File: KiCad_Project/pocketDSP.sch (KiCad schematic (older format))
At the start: 103 parts, among them IC1 TP4056, J2 USB_B_Micro, J3 SJ1-3525N, J4 SJ1-3525N, SW2 SW_SPDT, SW3 SW_SPDT, U1 3.5\"_TFT_LCD_SHILD_TOUCHSCRE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, U2 STM32H743VITx, U3 LMR62014XMF, U4 AP1117-33, U5 LM358, U6 CS5341, U7 CS4345, U8 LM358, Y1 25MHz

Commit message: V1.0
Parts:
- U5, U8: value LM358 -> OPA2340
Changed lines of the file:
@@
 P 7900 5700
 F 0 "U5" H 7900 6067 50  0000 C CNN
-F 1 "LM358" H 7900 5976 50  0000 C CNN
+F 1 "OPA2340" H 7900 5976 50  0000 C CNN
 F 2 "Package_SO:SOIC-8_3.9x4.9mm_P1.27mm" H 7900 5700 50  0001 C CNN
 F 3 "http://www.ti.com/lit/ds/symlink/lm2904-n.pdf" H 7900 5700 50  0001 C CNN
@@
 P 7900 4200
 F 0 "U5" H 7900 4550 50  0000 C CNN
-F 1 "LM358" H 7900 4450 50  0000 C CNN
+F 1 "OPA2340" H 7900 4450 50  0000 C CNN
 F 2 "Package_SO:SOIC-8_3.9x4.9mm_P1.27mm" H 7900 4200 50  0001 C CNN
 F 3 "http://www.ti.com/lit/ds/symlink/lm2904-n.pdf" H 7900 4200 50  0001 C CNN
@@
 P 6400 5650
 F 0 "U5" H 6358 5696 50  0000 L CNN
-F 1 "LM358" H 6358 5605 50  0000 L CNN
+F 1 "OPA2340" H 6358 5605 50  0000 L CNN
 F 2 "Package_SO:SOIC-8_3.9x4.9mm_P1.27mm" H 6400 5650 50  0001 C CNN
 F 3 "http://www.ti.com/lit/ds/symlink/lm2904-n.pdf" H 6400 5650 50  0001 C CNN
@@
 P 9900 5400
 F 0 "U8" H 9900 5767 50  0000 C CNN
-F 1 "LM358" H 9900 5676 50  0000 C CNN
+F 1 "OPA2340" H 9900 5676 50  0000 C CNN
 F 2 "Package_SO:SOIC-8_3.9x4.9mm_P1.27mm" H 9900 5400 50  0001 C CNN
 F 3 "http://www.ti.com/lit/ds/symlink/lm2904-n.pdf" H 9900 5400 50  0001 C CNN
@@
 P 9900 3900
 F 0 "U8" H 9900 4250 50  0000 C CNN
-F 1 "LM358" H 9900 4150 50  0000 C CNN
+F 1 "OPA2340" H 9900 4150 50  0000 C CNN
 F 2 "Package_SO:SOIC-8_3.9x4.9mm_P1.27mm" H 9900 3900 50  0001 C CNN
 F 3 "http://www.ti.com/lit/ds/symlink/lm2904-n.pdf" H 9900 3900 50  0001 C CNN
@@
 P 12450 5800
 F 0 "U8" H 12408 5846 50  0000 L CNN
-F 1 "LM358" H 12408 5755 50  0000 L CNN
+F 1 "OPA2340" H 12408 5755 50  0000 L CNN
 F 2 "Package_SO:SOIC-8_3.9x4.9mm_P1.27mm" H 12450 5800 50  0001 C CNN
 F 3 "http://www.ti.com/lit/ds/symlink/lm2904-n.pdf" H 12450 5800 50  0001 C CNN

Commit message: v1.0
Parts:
- L2, L3: footprint Inductor_SMD:L_1210_3225Metric_Pad1.42x2.65mm_HandSolder -> Inductor_SMD:L_Coilcraft_LPS5030
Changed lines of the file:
@@
 F 0 "L3" V 1290 10400 50  0000 C CNN
 F 1 "10uH" V 1199 10400 50  0000 C CNN
-F 2 "Inductor_SMD:L_1210_3225Metric_Pad1.42x2.65mm_HandSolder" H 1100 10400 50  0001 C CNN
+F 2 "Inductor_SMD:L_Coilcraft_LPS5030" H 1100 10400 50  0001 C CNN
 F 3 "~" H 1100 10400 50  0001 C CNN
 	1    1100 10400
@@
 F 0 "L2" V 3140 8800 50  0000 C CNN
 F 1 "10uH" V 3049 8800 50  0000 C CNN
-F 2 "Inductor_SMD:L_1210_3225Metric_Pad1.42x2.65mm_HandSolder" H 2950 8800 50  0001 C CNN
+F 2 "Inductor_SMD:L_Coilcraft_LPS5030" H 2950 8800 50  0001 C CNN
 F 3 "~" H 2950 8800 50  0001 C CNN
 	1    2950 8800

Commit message: v1.1
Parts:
- removed C10, C24, C7, C8, C9: 100nF, Capacitor_SMD:C_0402_1005Metric, symbol Device:C
- removed L3: 10uH, Inductor_SMD:L_Coilcraft_LPS5030, symbol Device:L
- added J1, J5: Conn_01x01, TestPoint:TestPoint_Pad_3.0x3.0mm, symbol Connector_Generic:Conn_01x01
- added MK1: Mic, Connector_Audio:CUI_CMA-6542PF, symbol Device:Microphone_Condenser
- added R26, R27: 100k, Resistor_SMD:R_0805_2012Metric_Pad1.15x1.40mm_HandSolder, symbol Device:R
- added SW1: SW_Push, Button_Switch_SMD:SW_SPST_CK_KXT3, symbol Switch:SW_Push
- C1, C13, C14, C15, C17, C18, C2, C20, C22, C26, C28, C29, C30, C31, C32, C33, C34, C35, C36, C37, C38, C39, C4, C40, C41, C42, C43, C44, C45, C46, C47, C48, C49, C5, C50, C51, C52, C53, C54: footprint Capacitor_SMD:C_0402_1005Metric -> Capacitor_SMD:C_0805_2012Metric_Pad1.15x1.40mm_HandSolder
- C12, C16, C19, C25: value 2.2uF -> 10uF
- C21: value 100nF -> 10uF; footprint Capacitor_SMD:C_0402_1005Metric -> Capacitor_SMD:C_0805_2012Metric_Pad1.15x1.40mm_HandSolder
- C23: value 2.2uF -> 100n
- C3, C6: value 100n -> 10uF; footprint Capacitor_SMD:C_0402_1005Metric -> Capacitor_SMD:C_0805_2012Metric_Pad1.15x1.40mm_HandSolder
- L1: value 10uH -> 1uH
- R1, R11, R12, R13, R14, R15, R16, R17, R18, R19, R2, R20, R21, R22, R23, R24, R25, R3, R4, R5, R6, R7, R8, R9: footprint Resistor_SMD:R_0402_1005Metric -> Resistor_SMD:R_0805_2012Metric_Pad1.15x1.40mm_HandSolder
- R10: value 3.3k -> 2.2k; footprint Resistor_SMD:R_0402_1005Metric -> Resistor_SMD:R_0805_2012Metric_Pad1.15x1.40mm_HandSolder
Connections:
- net +3V3: now also R26.1
- net +5V: now also U4.3 (VI)
- net ADC_AINL: now also C42.2, R18.1, R20.2; no longer C41.2, R17.1, R19.2
- net ADC_AINR: now also C41.2, R17.1, R19.2; no longer C42.2, R18.1, R20.2
- net ADC_M1: now also U2.57 (PD10); no longer U2.56 (PD9)
- net ADC_RST: now also U2.56 (PD9); no longer U2.57 (PD10)
- net GND: now also J5.1 (Pin_1), MK1.1 (-), R27.1, SW1.1
- net L_IN: now also C36.2, R12.2; no longer C35.2, R11.2
- net L_OUT: now also J4.3; no longer J4.2
- net R_IN: now also C35.2, R11.2; no longer C36.2, R12.2
- net R_OUT: now also J4.2; no longer J4.3
- net USB_5V: now also D2.2 (A), D4.2 (A); no longer R6.1, R9.1
- net at C15.1, U2.14 (NRST): now also SW1.2
- net MIC_IN: now reaches U2.16 (PC1)
- net MIC_IN: now also MK1.2 (+), R26.2, R27.2
- net at IC1.6 (STDBY): now also R9.2; no longer D4.1 (K)
- net at IC1.7 (CHRG): now also R6.2; no longer D2.1 (K)
- net at BT1.+, F1.2: now also J1.1 (Pin_1)
- new net: D2.1 (K), R6.1
- new net: D4.1 (K), R9.1
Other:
- moved on the sheet: C23, D2, D4, R6, R9

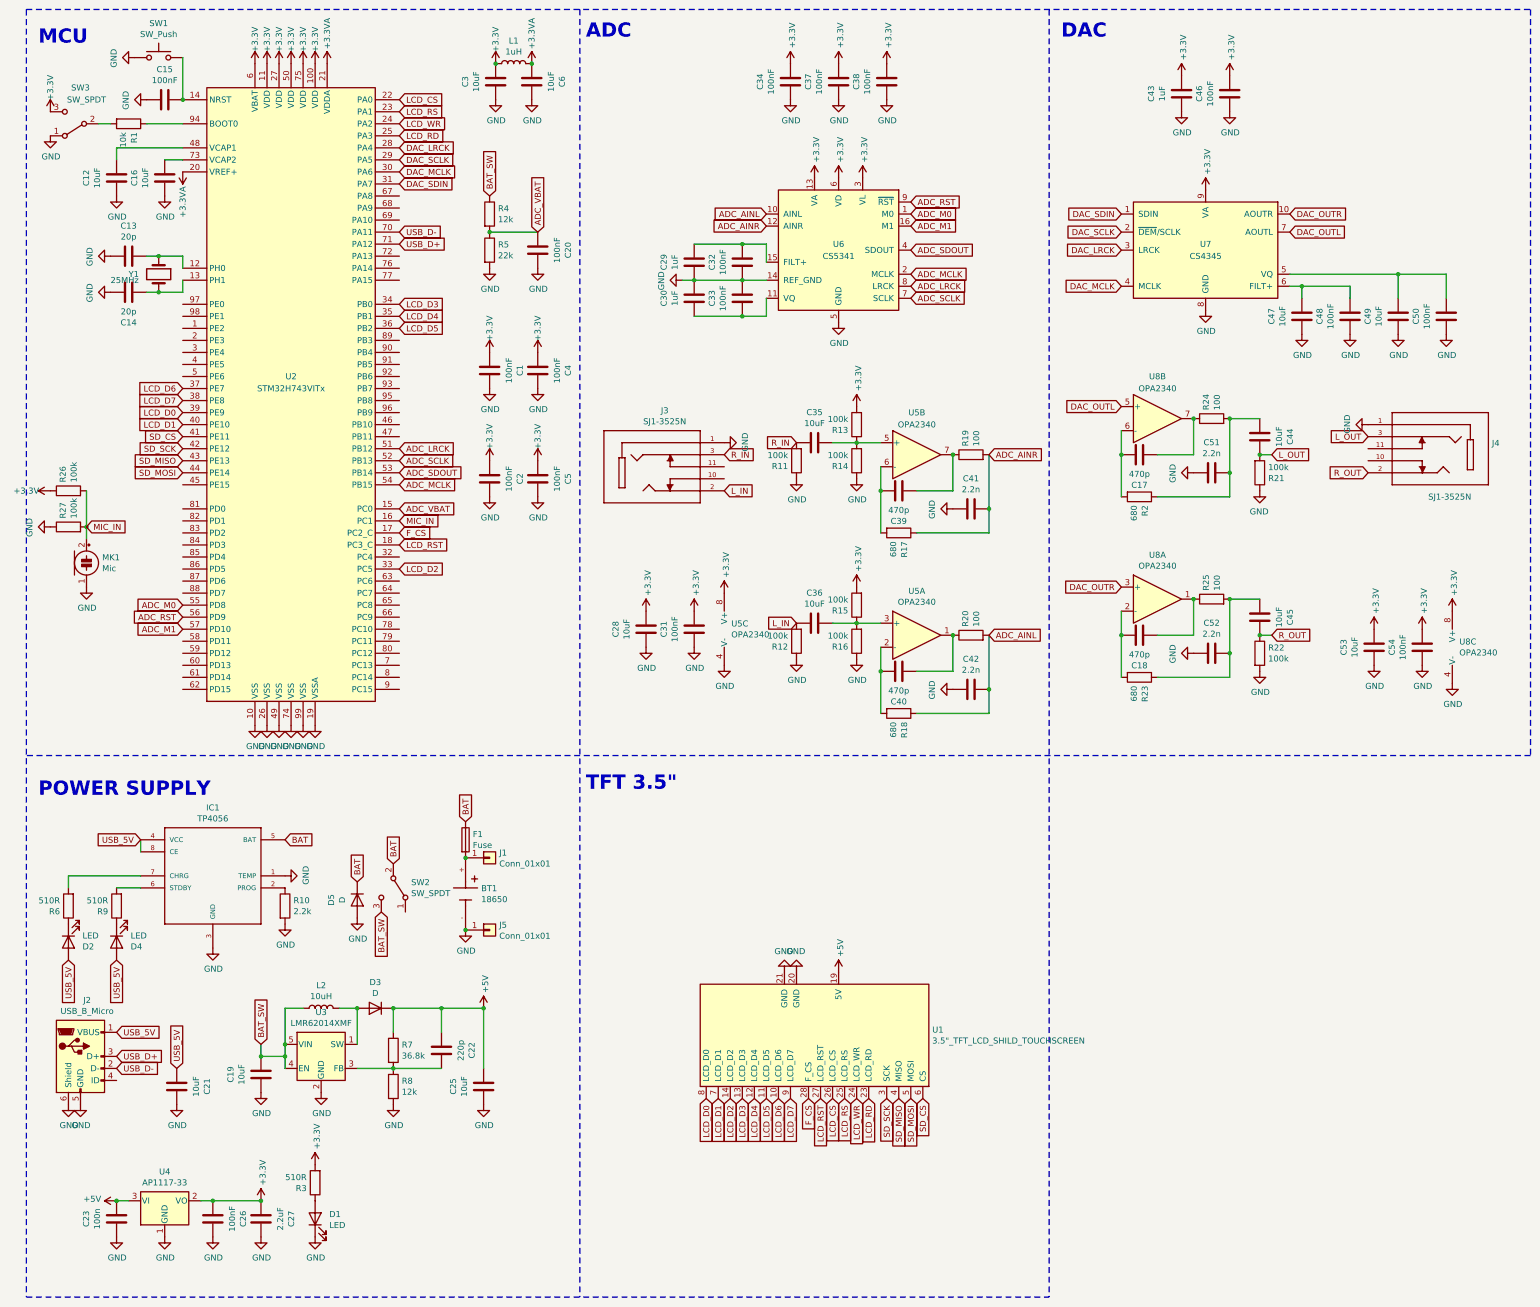
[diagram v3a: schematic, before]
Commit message: PCB v1.1
- Reduced DC/DC Converter ripple
- Added on PCB microphone
- Changed SMD from 0402 to 0805
- Improved total SNR
- Added reset push button
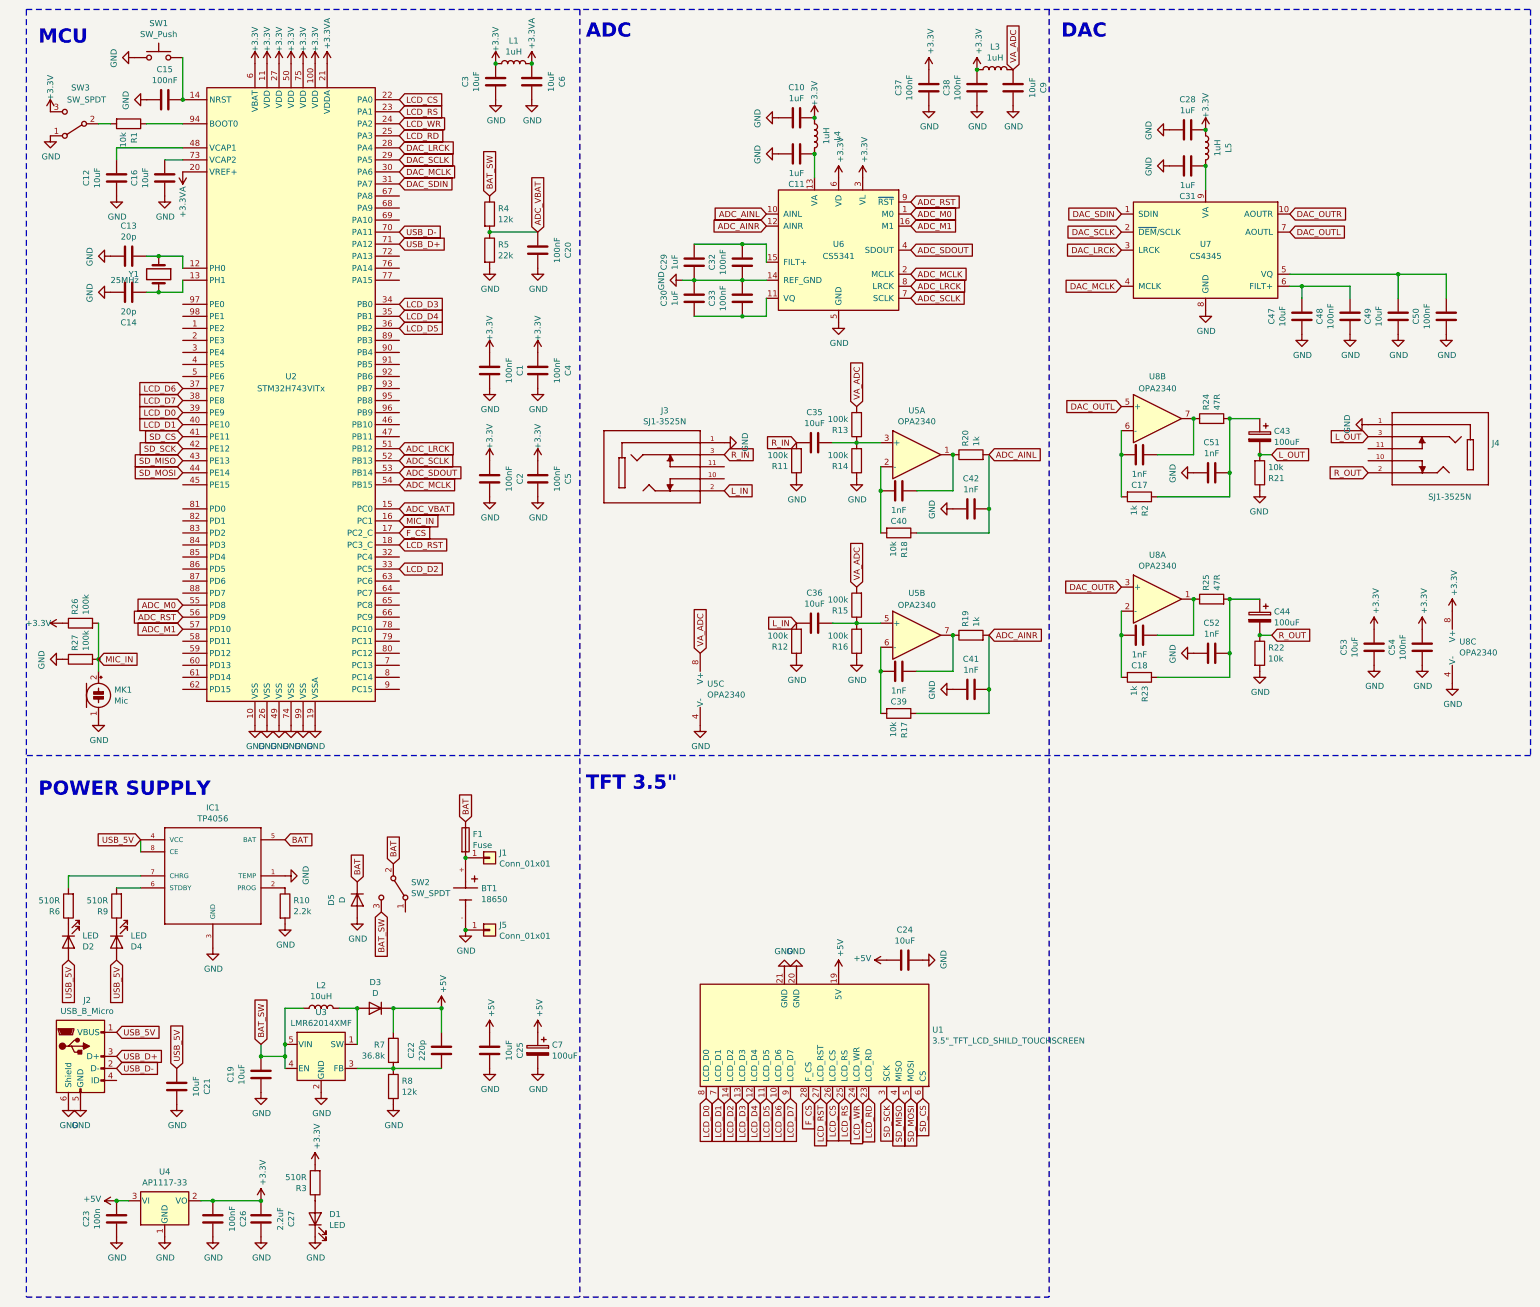
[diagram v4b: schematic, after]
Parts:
- removed C34, C46: 100nF, Capacitor_SMD:C_0805_2012Metric_Pad1.15x1.40mm_HandSolder, symbol Device:C
- removed C43: 1uF, Capacitor_SMD:C_0805_2012Metric_Pad1.15x1.40mm_HandSolder, symbol Device:C
- removed C44, C45: 10uF, Capacitor_SMD:C_0805_2012Metric_Pad1.15x1.40mm_HandSolder, symbol Device:C
- added C10, C11: 1uF, Capacitor_SMD:C_0805_2012Metric_Pad1.15x1.40mm_HandSolder, symbol Device:C
- added C24, C9: 10uF, Capacitor_SMD:C_0805_2012Metric_Pad1.15x1.40mm_HandSolder, symbol Device:C
- added C43, C44, C7: 100uF, Capacitor_Tantalum_SMD:CP_EIA-3216-18_Kemet-A_Pad1.58x1.35mm_HandSolder, symbol Device:CP
- added L3, L4, L5: 1uH, Inductor_SMD:L_0805_2012Metric_Pad1.15x1.40mm_HandSolder, symbol Device:L
- C17, C18, C39, C40: value 470p -> 1nF
- C28: value 10uF -> 1uF
- C31: value 100nF -> 1uF
- C41, C42, C51, C52: value 2.2n -> 1nF
- R17, R18: value 680 -> 10k
- R19, R20: value 100 -> 1k
- R2, R23: value 680 -> 1k
- R21, R22: value 100k -> 10k
- R24, R25: value 100 -> 47R
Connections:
- net +3V3: now also C10.1, L3.1, L4.1, L5.1; no longer C31.1, R13.2, R15.2, U5.8 (V+), U6.13 (VA), U7.9 (VA)
- net +5V: now also C24.1, C7.1
- net GND: now also C31.1, C10.2, C11.1, C24.2, C7.2, C9.1; no longer C31.2
- net L_OUT: now also C43.2
- net R_OUT: now also C44.2
- net at C52.2, R23.1, R25.2: now also C44.1
- net at C51.2, R2.1, R24.2: now also C43.1
- net at C36.1, R15.1, R16.2: now also U5.5 (+); no longer U5.3 (+)
- net at C35.1, R13.1, R14.2: now also U5.3 (+); no longer U5.5 (+)
- new net: C31.2, L5.2, U7.9 (VA)
- new net: C11.2, L4.2, U6.13 (VA)
- new net VA_ADC: C9.2, L3.2, R13.2, R15.2, U5.8 (V+)
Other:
- moved on the sheet: C25, C37, C38, C39, C40, C41, C42, MK1, R17, R18, R19, R20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
